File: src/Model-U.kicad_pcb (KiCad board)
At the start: 2 copper layers, 20 x 13.5 mm, 5 parts, among them J1 USB_C_Receptacle, J2 Conn_01x04, J3 Conn_01x04

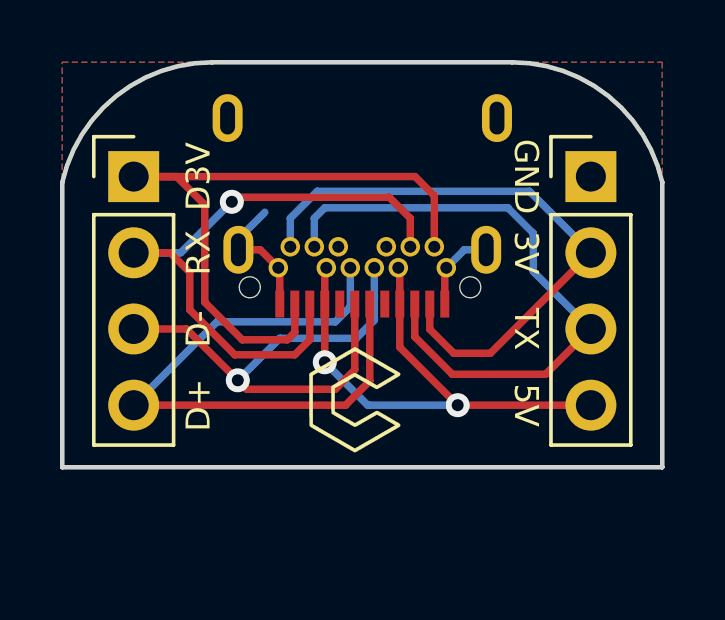
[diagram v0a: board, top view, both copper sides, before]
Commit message: Model U v2
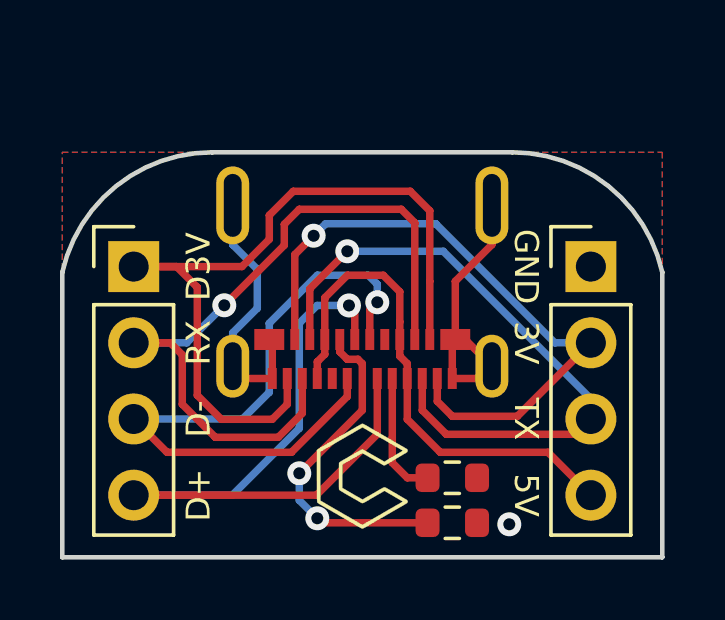
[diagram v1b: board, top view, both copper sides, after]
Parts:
- removed the G*** at (-0.25, 8.25)
- removed the G*** at (136.9, 121.4)
- added G***: LOGO, Model_S:USBC_C_Logo, F.Cu at (0.00, 10.8)
- added R1: R, Resistor_SMD:R_0603_1608Metric, F.Cu at (3.00, 10.8)
- added R2: R, Resistor_SMD:R_0603_1608Metric, F.Cu at (3.00, 12.3)
- J1: footprint Model_S:Shou Han Type-C 24P QCHT -> Model_S:1054500101
- moved J1 3.00 mm to (0.00, 0.00)
- moved J2 3.00 mm to (-7.62, 3.81)
- moved J3 3.00 mm to (7.62, 3.81)
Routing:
- net Net-(J1-PadB5): track 0.00 -> 11.3 mm, vias 0 -> 2
- net GND: track 7.23 -> 18.3 mm, vias 0 -> 1
- net RX-: track 20.6 -> 25.1 mm
- net D-: track 18.0 -> 22.5 mm
- net Net-(J1-PadA5): track 0.00 -> 4.19 mm
- net D3V: track 22.6 -> 26.3 mm
- net D+: track 20.6 -> 23.9 mm, vias 0 -> 1
- net 3V3: track 20.1 -> 21.9 mm, vias 0 -> 1
- net VBUS: track 18.0 -> 17.4 mm, vias 2 -> 0
- net TX-: track 20.8 -> 21.5 mm, vias 0 -> 1
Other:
- board text added: "v2"
- board text removed: "v1"

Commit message: Model U v3
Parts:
- J1: footprint Model_S:1054500101 -> Model_S:Shou Han Type-C 24P QCHT
- turned R2 to 180 degrees
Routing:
- net GND: track 18.3 -> 26.7 mm
- net Net-(J1-PadB5): track 11.3 -> 15.2 mm, vias 2 -> 1
- net VBUS: track 17.4 -> 20.0 mm, vias 0 -> 1
- net D+: track 23.9 -> 25.9 mm, vias 1 -> 0
- net D-: track 22.5 -> 21.1 mm, vias 1 -> 0
- net 3V3: track 21.9 -> 20.9 mm
- net D3V: track 26.3 -> 25.4 mm
- net TX-: track 21.5 -> 20.9 mm
- removed copper zone on F.Cu, net GND
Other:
- board text added: "v3"
- board text removed: "v2"
